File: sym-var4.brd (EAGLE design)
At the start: 54 x 31.5 mm, 23 parts, among them SW1 SPST_TACT-KMR2, U1 L9110, U2 L9110, U3 ESP8266MODULES_ESP12E, U4 AP2112K-3.3V, U5 ALC5628

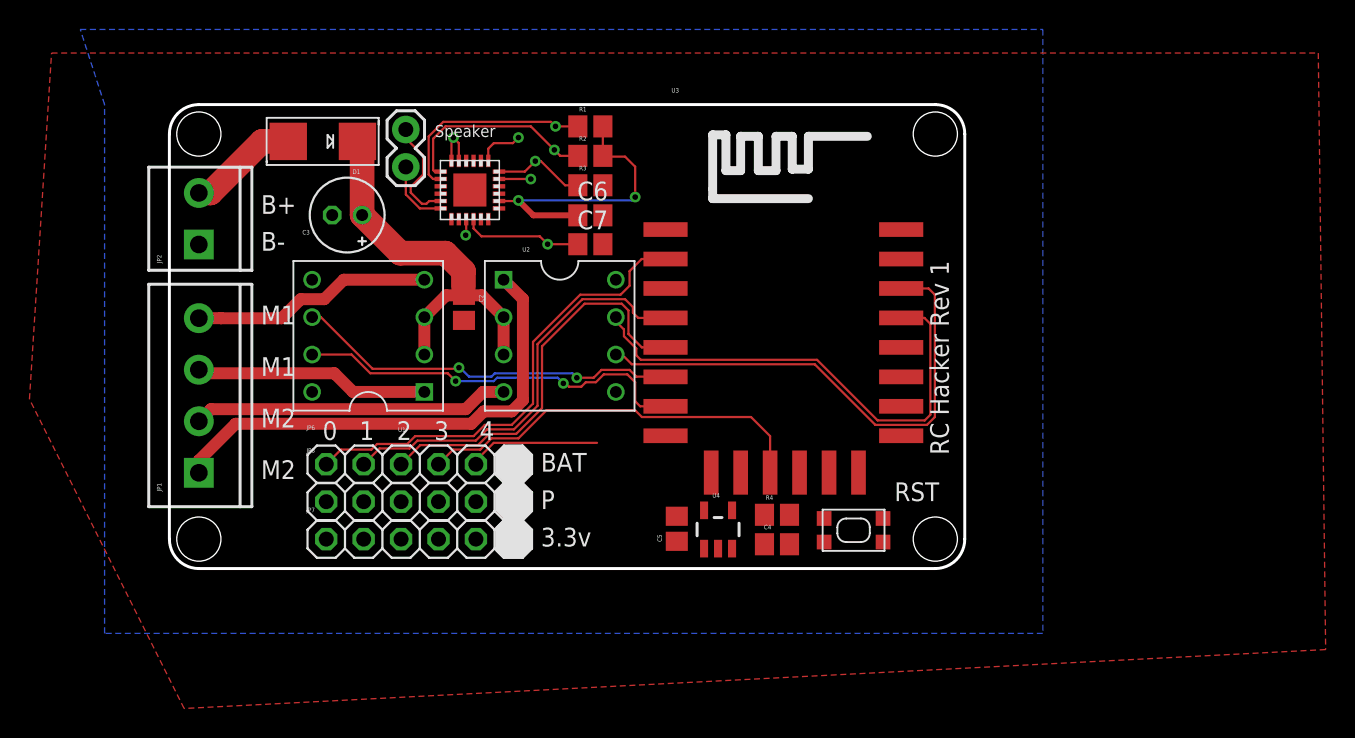
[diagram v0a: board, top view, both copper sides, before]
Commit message: Added Prog Connector
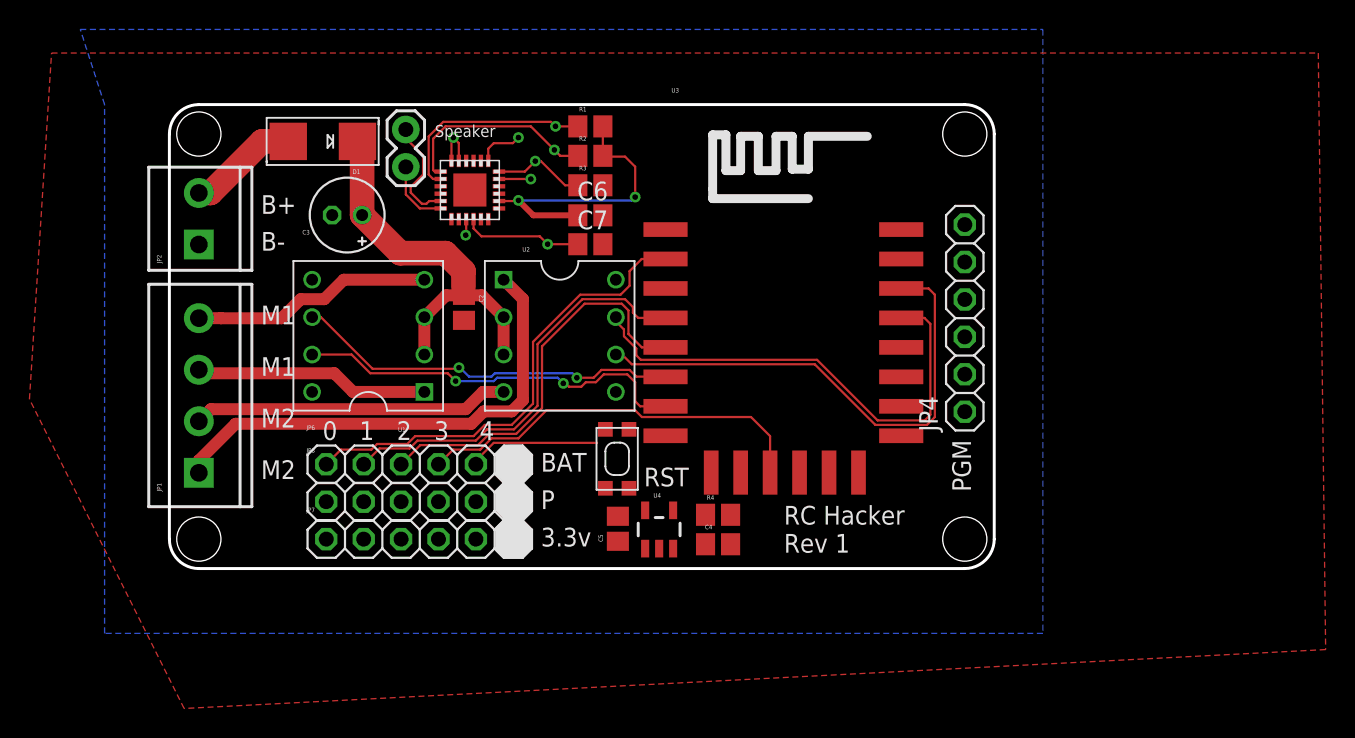
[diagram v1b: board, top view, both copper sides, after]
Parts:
- added JP4: (no value), adafruit:1X06
- moved SW1 16.8 mm to (30.4, 7.45), turned to 270 degrees
- moved C5 4.00 mm to (30.4, 2.70)
- moved C4 4.00 mm to (37.2, 1.65)
- moved R4 4.00 mm to (37.2, 3.65)
- moved U4 4.00 mm to (33.2, 2.65)
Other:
- board size 54 x 31.5 mm -> 56 x 31.5 mm
- board text added: "PGM"
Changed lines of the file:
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@@
 <setting verticaltext="up"/>
 </settings>
-<grid distance="3" unitdist="mil" unit="mil" style="lines" multiple="1" display="yes" altdistance="0.025" altunitdist="inch" altunit="inch"/>
+<grid distance="1" unitdist="mm" unit="mm" style="lines" multiple="1" display="yes" altdistance="0.025" altunitdist="inch" altunit="inch"/>
 <layers>
 <layer number="1" name="Top" color="4" fill="1" visible="yes" active="yes"/>
@@
 <wire x1="0" y1="2" x2="0" y2="29.5" width="0.2" layer="20"/>
 <wire x1="0" y1="29.5" x2="2" y2="31.5" width="0.2" layer="20" curve="-90"/>
-<wire x1="2" y1="31.5" x2="52" y2="31.5" width="0.2" layer="20"/>
-<wire x1="52" y1="31.5" x2="54" y2="29.5" width="0.2" layer="20" curve="-90"/>
-<wire x1="54" y1="29.5" x2="54" y2="2" width="0.2" layer="20"/>
-<wire x1="54" y1="2" x2="52" y2="0" width="0.2" layer="20" curve="-90"/>
-<wire x1="52" y1="0" x2="2" y2="0" width="0.2" layer="20"/>
+<wire x1="2" y1="31.5" x2="54" y2="31.5" width="0.2" layer="20"/>
+<wire x1="54" y1="31.5" x2="56" y2="29.5" width="0.2" layer="20" curve="-90"/>
+<wire x1="56" y1="29.5" x2="56" y2="2" width="0.2" layer="20"/>
+<wire x1="56" y1="2" x2="54" y2="0" width="0.2" layer="20" curve="-90"/>
+<wire x1="54" y1="0" x2="2" y2="0" width="0.2" layer="20"/>
 <wire x1="0" y1="32.5" x2="54" y2="32.5" width="0.2" layer="90"/>
 <wire x1="-3" y1="27.5" x2="-3" y2="0" width="0.2" layer="90"/>
@@
 <hole x="2" y="2" drill="3"/>
 <hole x="2" y="29.5" drill="3"/>
-<hole x="52" y="2" drill="3"/>
-<hole x="52" y="29.5" drill="3"/>
+<hole x="54" y="2" drill="3"/>
+<hole x="54" y="29.5" drill="3"/>
 <text x="18.0193625" y="29.3" size="0.8128" layer="21" font="vector">Speaker</text>
 <text x="11.4" y="10" size="1.27" layer="21" font="vector" rot="R180">0</text>
@@
 <text x="6.22" y="9.58" size="1.27" layer="21" font="vector">M2</text>
 <text x="6.22" y="6.08" size="1.27" layer="21" font="vector">M2</text>
-<text x="49.22" y="4.58" size="1.27" layer="21" font="vector">RST</text>
-<text x="52.92" y="7.72" size="1.27" layer="21" font="vector" rot="R90">RC Hacker Rev 1</text>
+<text x="32.22" y="5.58" size="1.27" layer="21" font="vector">RST</text>
+<text x="41.72" y="1.08" size="1.27" layer="21" font="vector">RC Hacker
+Rev 1</text>
+<text x="54.42" y="5.22" size="1.27" layer="21" font="vector" rot="R90">PGM</text>
 </plain>
 <attributes>
@@
 <attribute name="VALUE" x="27.8168" y="19.7334" size="1.27" layer="27"/>
 </element>
-<element name="U4" library="SparkFun-PowerIC" package="SOT23-5" value="AP2112K-3.3V" x="37.25" y="2.6524" smashed="yes">
-<attribute name="PROD_ID" value="VREG-12457" x="33.44" y="9.0024" size="1.778" layer="27" display="off"/>
-<attribute name="NAME" x="36.861" y="4.8114" size="0.3048" layer="25" font="vector"/>
-<attribute name="VALUE" x="36.7975" y="2.4619" size="0.4064" layer="27"/>
+<element name="U4" library="SparkFun-PowerIC" package="SOT23-5" value="AP2112K-3.3V" x="33.25" y="2.6524" smashed="yes">
+<attribute name="PROD_ID" value="VREG-12457" x="29.44" y="9.0024" size="1.778" layer="27" display="off"/>
+<attribute name="NAME" x="32.861" y="4.8114" size="0.3048" layer="25" font="vector"/>
+<attribute name="VALUE" x="32.7975" y="2.4619" size="0.4064" layer="27"/>
 </element>
 <element name="C3" library="rcl" package="E2-5" value="" x="12.0693625" y="24" smashed="yes" rot="R180">
@@
 <attribute name="VALUE" x="12.959359375" y="31.286" size="0.4064" layer="27" font="vector" rot="R180"/>
 </element>
-<element name="R4" library="rcl" package="R0805" value="330" x="41.25" y="3.65" smashed="yes">
-<attribute name="NAME" x="40.488" y="4.666" size="0.3048" layer="25" font="vector"/>
-<attribute name="VALUE" x="40.488" y="1.364" size="1.27" layer="27"/>
-</element>
-<element name="C4" library="adafruit" package="C0805" value="" x="41.25" y="1.65" smashed="yes">
-<attribute name="NAME" x="40.361" y="2.666" size="0.3048" layer="25" font="vector"/>
-<attribute name="VALUE" x="40.361" y="-0.636" size="1.27" layer="27"/>
-</element>
-<element name="C5" library="adafruit" package="C0805" value="" x="34.45" y="2.7" smashed="yes" rot="R90">
-<attribute name="NAME" x="33.434" y="1.811" size="0.3048" layer="25" font="vector" rot="R90"/>
-<attribute name="VALUE" x="36.736" y="1.811" size="1.27" layer="27" rot="R90"/>
+<element name="R4" library="rcl" package="R0805" value="330" x="37.25" y="3.65" smashed="yes">
+<attribute name="NAME" x="36.488" y="4.666" size="0.3048" layer="25" font="vector"/>
+<attribute name="VALUE" x="36.488" y="1.364" size="1.27" layer="27"/>
+</element>
+<element name="C4" library="adafruit" package="C0805" value="" x="37.25" y="1.65" smashed="yes">
+<attribute name="NAME" x="36.361" y="2.666" size="0.3048" layer="25" font="vector"/>
+<attribute name="VALUE" x="36.361" y="-0.636" size="1.27" layer="27"/>
+</element>
+<element name="C5" library="adafruit" package="C0805" value="" x="30.45" y="2.7" smashed="yes" rot="R90">
+<attribute name="NAME" x="29.434" y="1.811" size="0.3048" layer="25" font="vector" rot="R90"/>
+<attribute name="VALUE" x="32.736" y="1.811" size="1.27" layer="27" rot="R90"/>
 </element>
 <element name="JP6" library="adafruit" package="1X06" value="" x="17" y="7.08" smashed="yes">
@@
 <attribute name="NAME" x="34.0835" y="32.3155" size="0.3048" layer="25" font="vector"/>
 </element>
-<element name="SW1" library="adafruit" package="KMR2" value="SPST_TACT-KMR2" x="46.45" y="2.6" smashed="yes" rot="R180"/>
+<element name="SW1" library="adafruit" package="KMR2" value="SPST_TACT-KMR2" x="30.4" y="7.45" smashed="yes" rot="R270"/>
 <element name="U5" library="ALC5628" package="QFN24" value="ALC5628" x="20.4" y="25.7" rot="R180"/>
 <element name="JP3" library="SparkFun-Connectors" package="1X02" value="M02PTH" x="16.051640625" y="29.806359375" smashed="yes" rot="R270">
@@
 <element name="C6" library="adafruit" package="C0805" value="" x="28.5788" y="23.9806"/>
 <element name="C7" library="adafruit" package="C0805" value="" x="28.5788" y="22.0194"/>
+<element name="JP4" library="adafruit" package="1X06" value="" x="54" y="17" rot="R90"/>
 </elements>
 <signals>
@@
 <wire x1="19.65" y1="27.675" x2="22.375" y2="24.95" width="0" layer="19" extent="1-1"/>
 <wire x1="33.6835" y1="9.0155" x2="33.6835" y2="19.0155" width="0" layer="19" extent="1-1"/>
-<wire x1="36.3" y1="3.9525" x2="33.6835" y2="9.0155" width="0" layer="19" extent="1-1"/>
-<wire x1="34.45" y1="1.85" x2="36.3" y2="3.9525" width="0" layer="19" extent="1-1"/>
-<wire x1="40.4" y1="3.65" x2="36.3" y2="3.9525" width="0" layer="19" extent="1-1"/>
+<wire x1="32.3" y1="3.9525" x2="33.6835" y2="9.0155" width="0" layer="19" extent="1-1"/>
+<wire x1="30.45" y1="1.85" x2="32.3" y2="3.9525" width="0" layer="19" extent="1-1"/>
+<wire x1="36.4" y1="3.65" x2="32.3" y2="3.9525" width="0" layer="19" extent="1-1"/>
 </signal>
 <signal name="ESP_RXD">
@@
 <wire x1="13.0853625" y1="24" x2="15.6731625" y2="21.4122" width="1.6764" layer="1"/>
 <wire x1="15.6731625" y1="21.4122" x2="18.7452" y2="21.4122" width="1.6764" layer="1"/>
-<wire x1="36.3" y1="1.3523" x2="38.2" y2="1.3523" width="0" layer="19" extent="1-1"/>
-<wire x1="40.4" y1="1.65" x2="38.2" y2="1.3523" width="0" layer="19" extent="1-1"/>
-<wire x1="22.69" y1="14.53" x2="36.3" y2="1.3523" width="0" layer="19" extent="1-1"/>
+<wire x1="34.2" y1="1.3523" x2="36.4" y2="1.65" width="0" layer="19" extent="1-1"/>
+<wire x1="32.3" y1="1.3523" x2="34.2" y2="1.3523" width="0" layer="19" extent="1-1"/>
+<wire x1="22.69" y1="14.53" x2="32.3" y2="1.3523" width="0" layer="19" extent="1-1"/>
 </signal>
 <signal name="1A">
@@
 <contactref element="SW1" pad="1"/>
 <contactref element="SW1" pad="3"/>
-<wire x1="42.1" y1="3.65" x2="33.6835" y2="23.0155" width="0" layer="19" extent="1-1"/>
-<wire x1="44.45" y1="1.8" x2="42.1" y2="3.65" width="0" layer="19" extent="1-1"/>
-<wire x1="48.45" y1="1.8" x2="44.45" y2="1.8" width="0" layer="19" extent="1-1"/>
+<wire x1="31.2" y1="9.45" x2="33.6835" y2="23.0155" width="0" layer="19" extent="1-1"/>
+<wire x1="31.2" y1="5.45" x2="31.2" y2="9.45" width="0" layer="19" extent="1-1"/>
+<wire x1="38.1" y1="3.65" x2="31.2" y2="5.45" width="0" layer="19" extent="1-1"/>
 </signal>
 <signal name="N$1">
@@
 </board>
 </drawing>
+<compatibility>
+<note version="6.3" minversion="6.2.2" severity="warning">
+Since Version 6.2.2 text objects can contain more than one line,
+which will not be processed correctly with this version.
+</note>
+</compatibility>
 </eagle>

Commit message: Layout complete
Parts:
- moved C5 1.17 mm to (29.6, 3.45), turned to 180 degrees
- moved SW1 0.75 mm to (29.6, 7.45)
- moved U4 0.75 mm to (33.2, 3.40)
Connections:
- new net N$9: JP8.1, JP8.2, JP8.3, JP8.4, JP8.5, JP8.6
- net +3V3: now also JP7.6
- net ESP_RXD: now also JP4.3
- net ESP_TXD: now also JP4.2
- net GND: now also JP4.6, JP7.1, JP7.2, JP7.3, JP7.4, JP7.5
- net GPIO0: now also JP4.1
- net VBAT: now also JP6.6
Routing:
- net +3V3: track 25.1 -> 84.8 mm, vias 4 -> 6
- net ESP_TXD: track 2.27 -> 54.3 mm, vias 1 -> 2
- net GPIO0: track 14.3 -> 56.8 mm, vias 1 -> 2
- net ESP_RXD: track 3.27 -> 45.2 mm, vias 1 -> 2
- net VBAT: track 26.9 -> 67.9 mm, vias 0 -> 1
- net GPIO15: track 6.40 -> 44.2 mm, vias 1 -> 2
- net GPIO2: track 13.8 -> 49.1 mm, vias 1 -> 2
- net RST: track 0.00 -> 31.3 mm, vias 0 -> 2
- net GPIO10: track 8.92 -> 31.7 mm, vias 0 -> 2
- net N$9: track 0.00 -> 12.7 mm
- net 2B: track 33.4 -> 22.8 mm, vias 0 -> 2
- net 2A: track 34.6 -> 24.5 mm, vias 0 -> 2
- net ADC: track 31.8 -> 39.3 mm
- net GPIO9: track 27.2 -> 28.9 mm
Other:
- board text removed: "BAT"
